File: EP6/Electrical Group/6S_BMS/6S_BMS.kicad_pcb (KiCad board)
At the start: 4 copper layers, 100 x 70 mm, 180 parts, among them IC1 DZDH0401DW-7, J1 Cell Pads, J2 24V_OUT, J3 CHARGE, J4 HVB_Front_Panel, J5 UART, J6 I2C, J7 SWD, J8 USB_C_stm32, Q1 HSBA3119, Q10 SI2301CDS-T1-GE3, Q11 SI2301CDS-T1-GE3, Q12 SI2301CDS-T1-GE3, Q13 2N7002, Q14 AO3401A, Q2 2N7002, Q3 2N7002, Q4 HSBA3119, Q5 2N7002, Q6 HSBA3119, Q7 SI2301CDS-T1-GE3, Q8 SI2301CDS-T1-GE3, Q9 SI2301CDS-T1-GE3, SW1 RESET, U1 BQ7693003, U2 TCAN1042VDRQ1, U3 STM32F103C8Tx, U4 LM66100DCK, U5 CAT24C256, U6 78L05G-AB3-R, U7 HT7533, Y1 8MHz X49SM8MSD2SC

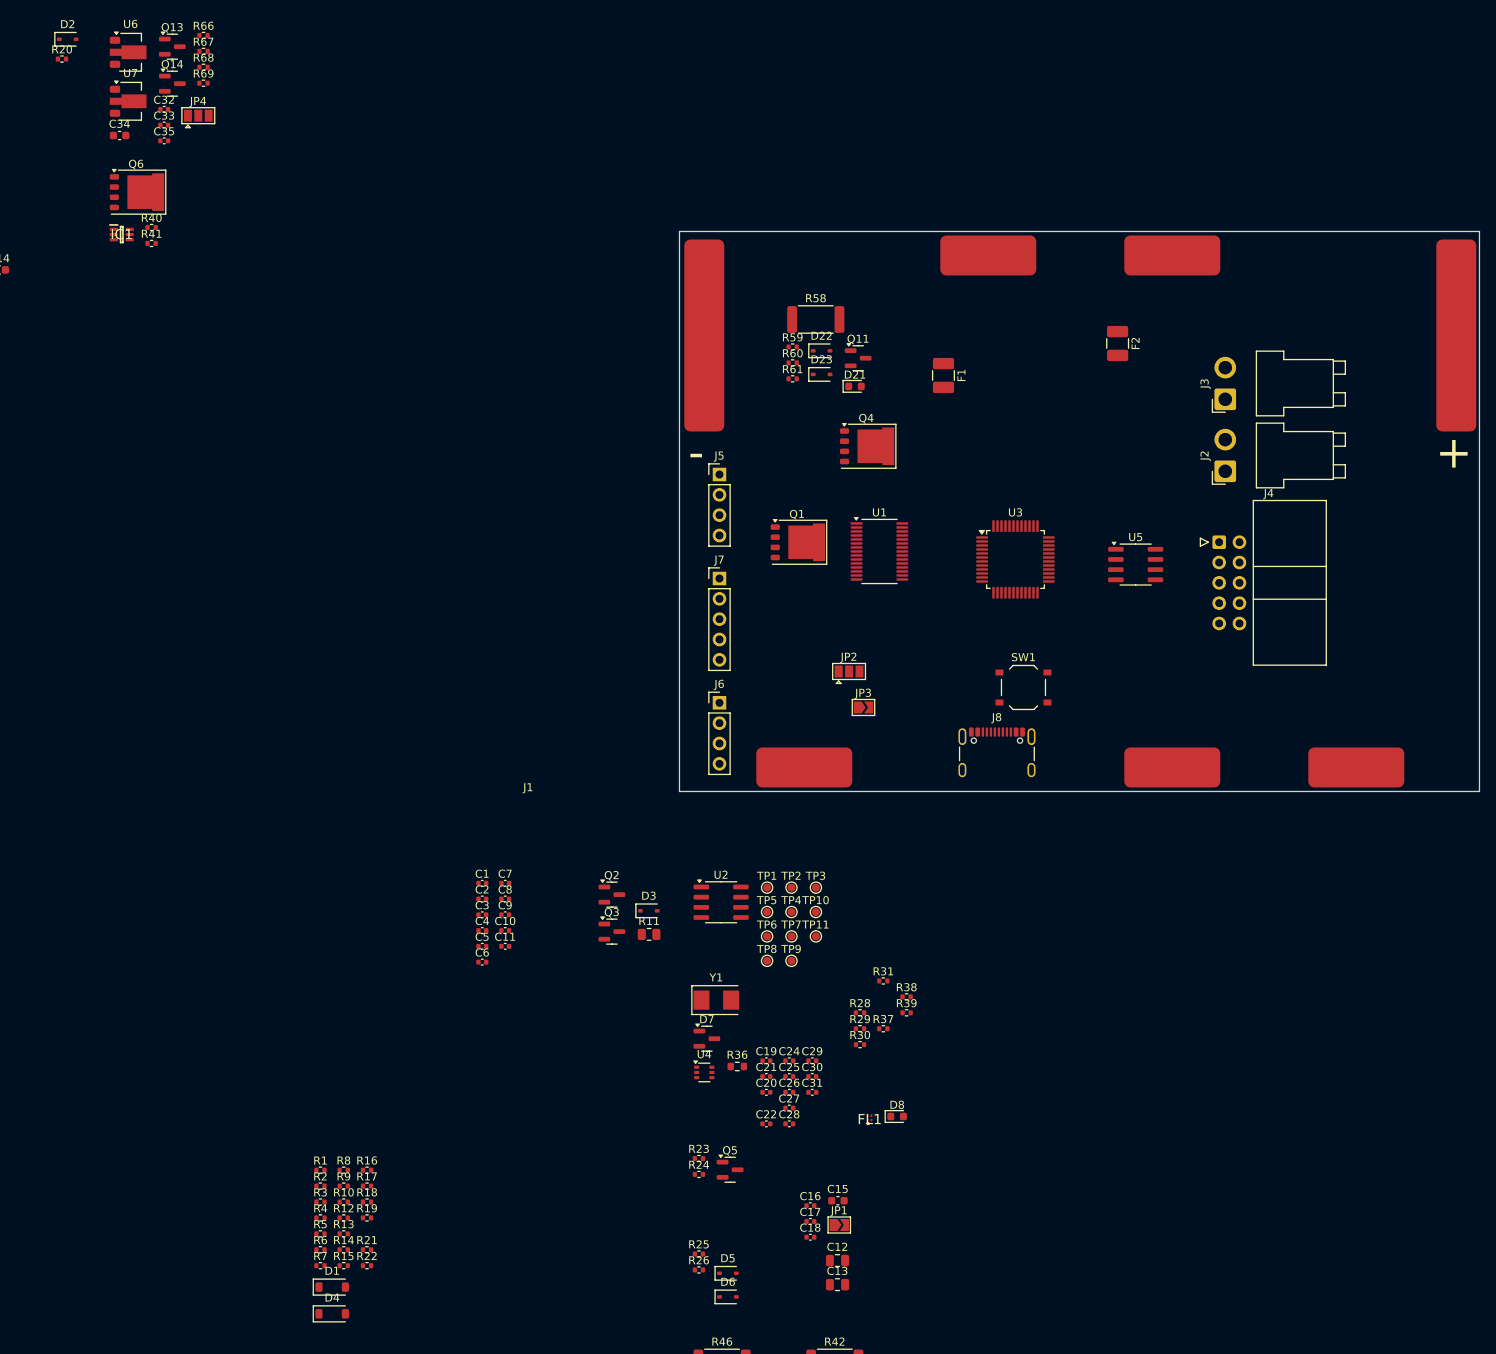
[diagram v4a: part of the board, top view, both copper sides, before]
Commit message: fix net ties and net classes
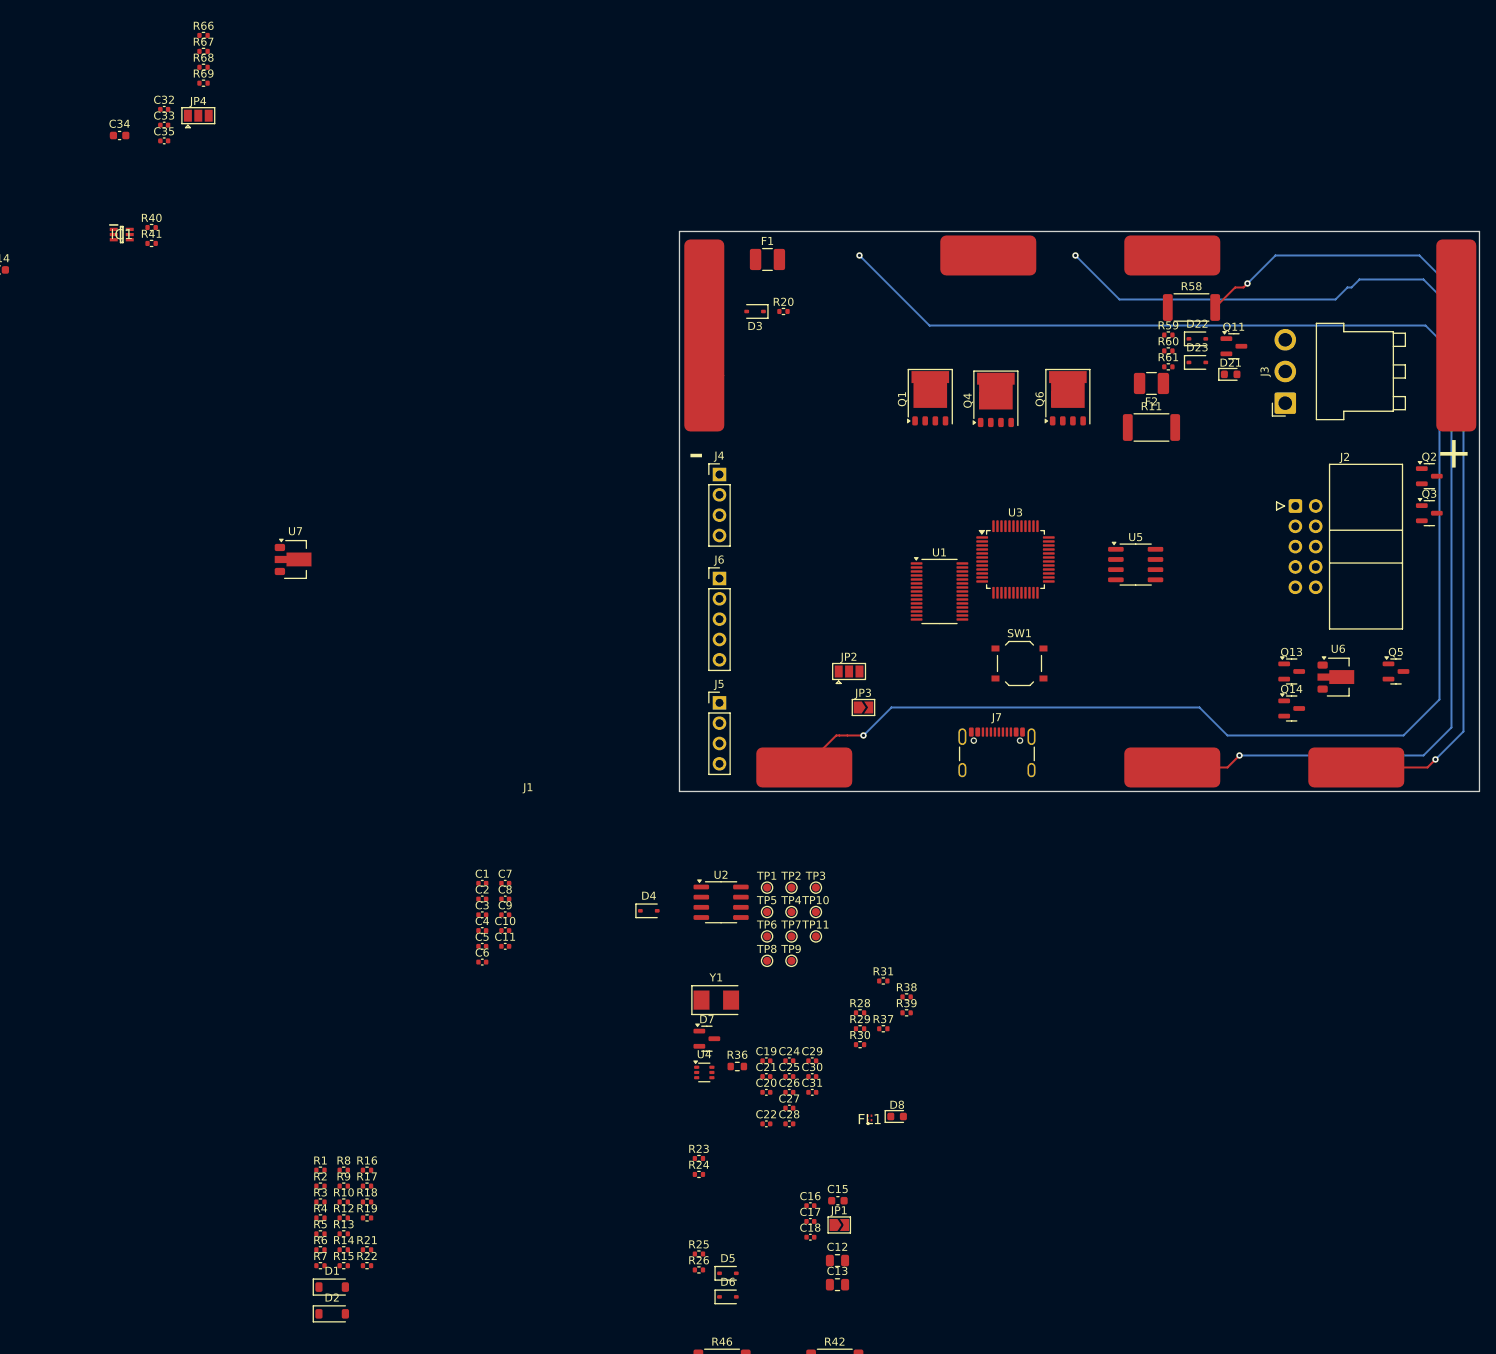
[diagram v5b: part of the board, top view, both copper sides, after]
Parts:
- removed the J4 at (167.5, 63.8)
- J2: value 24V_OUT -> Front Panel; footprint Connector_JST:JST_VH_B2PS-VH_1x02_P3.96mm_Horizontal -> Connector_IDC:IDC-Header_2x05_P2.54mm_Horizontal
- J3: value CHARGE -> Power; footprint Connector_JST:JST_VH_B2PS-VH_1x02_P3.96mm_Horizontal -> Connector_JST:JST_VH_B3PS-VH_1x03_P3.96mm_Horizontal
- R11: value 10R 1% -> 1m; footprint Resistor_SMD:R_0805_2012Metric -> Resistor_SMD:R_2512_6332Metric
- U6: value 78L05G-AB3-R -> L78L05_SOT89
- moved U6 170.0 mm to (182.3, 80.7)
- moved Q13 160.2 mm to (176.5, 80.0)
- moved Q14 160.2 mm to (176.5, 84.6)
- moved Q6 119.3 mm to (148.6, 46.0), turned to 90 degrees
- moved Q2 114.8 mm to (193.7, 55.6)
- moved Q3 114.8 mm to (193.7, 60.2)
- moved Q5 104.0 mm to (189.6, 80.0)
- moved R20 95.5 mm to (113.0, 35.0)
- moved D3 92.4 mm to (109.5, 35.0), turned to 180 degrees
- moved R11 89.2 mm to (159.0, 49.5)
- moved U7 60.9 mm to (52.0, 66.0)
- moved D22 47.0 mm to (164.7, 38.4)
- moved D23 47.0 mm to (164.7, 41.4)
- moved R59 47.0 mm to (161.1, 37.9)
- moved R60 47.0 mm to (161.1, 39.9)
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- renumbered D4 to D2, D2 to D3, D3 to D4, J5 to J4, J6 to J5, J7 to J6, J8 to J7
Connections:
- D1 pad 1: +24V -> /PACK+
- D5 pad 2: /AFE/VC5 -> /C3
- D6 pad 2: /AFE/VC10 -> /C6
- IC1 pad 4: +24V -> /PACK+
- J2 pad 1: /PACK- -> /MODE_BTN_A
- J2 pad 2: +24V -> /MODE_BTN_B
- J3 pad 2: /CHG_EXT -> /PACK+
- J5 pad 3: /MCU/I2C1_SCL -> /SCL
- J5 pad 4: /MCU/I2C1_SDA -> /SDA
- Q4 pad D: +24V -> /PACK+
- Q6 pad S: +24V -> /PACK+
- R11 pad 1: /CELLS- -> /CT0
- R9 pad 1: /CELLS- -> /CT0
- TP6 pad 1: /DISP_CS -> /MCU/SPI2_CS
- TP7 pad 1: /DISP_CLK -> /MCU/SPI2_SCK
- TP9 pad 1: /DISP_DIN -> /MCU/SPI2_MOSI
- U1 pad 16: /AFE/VC10 -> /C6
- U1 pad 22: /AFE/VC5 -> /C3
- U3 pad 25: /DISP_CS -> /MCU/SPI2_CS
- U3 pad 26: /DISP_CLK -> /MCU/SPI2_SCK
- U3 pad 28: /DISP_DIN -> /MCU/SPI2_MOSI
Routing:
- net /CT5: track 0.00 -> 207.7 mm, vias 0 -> 2
- net /CT3: track 0.00 -> 141.2 mm, vias 0 -> 2
- net /CT1: track 0.00 -> 105.3 mm, vias 0 -> 2
- net /CT6: track 0.00 -> 5.99 mm
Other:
- copper layers 4 -> 2

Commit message: switched back to xt60, changed shunt resistor
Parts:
- removed the J3 at (175.7, 46.5)
- added J2: Power Out, Connector_AMASS:AMASS_XT60PW-F_1x02_P7.20mm_Horizontal, F.Cu at (169.2, 65.0)
- added J4: Charge, Connector_AMASS:AMASS_XT60PW-M_1x02_P7.20mm_Horizontal, F.Cu at (169.2, 75.8)
- added NT1: NetTie_2, NetTie:NetTie-2_SMD_Pad0.5mm, B.Cu at (13.6, 56.9)
- C1, C10, C11, C12, C13, C14, C15, C16, C17, C18, C19, C2, C20, C21, C22, C23, C24, C25, C26, C27, C28, C29, C3, C30, C31, C32, C33, C34, C35, C4, C5, C6, C7, C8, C9, D1, D10, D11, D12, D13, D14, D15, D16, D17, D18, D19, D2, D20, D21, D22, D23, D24, D25, D26, D3, D4, D5, D6, D7, D8, D9, FL1, IC1, JP1, JP2, JP3, JP4, Q1, Q10, Q11, Q12, Q13, Q14, Q2, Q3, Q4, Q5, Q6, Q7, Q8, Q9, R1, R10, R12, R13, R14, R15, R16, R17, R18, R19, R2, R20, R21, R22, R23, R24, R25, R26, R27, R28, R29, R3, R30, R31, R32, R33, R34, R35, R36, R37, R38, R39, R4, R40, R41, R42, R43, R44, R45, R46, R47, R48, R49, R5, R50, R51, R52, R53, R54, R55, R56, R57, R58, R59, R6, R60, R61, R62, R63, R64, R65, R66, R67, R68, R69, R7, R8, R9, SW1, TP1, TP10, TP11, TP2, TP3, TP4, TP5, TP6, TP7, TP8, TP9, U1, U2, U3, U4, U5, U6, U7, Y1: moved to B.Cu
- J8: renamed from J7; moved to B.Cu
- R11: value 1m -> 10m; moved to B.Cu
- moved R27 240.1 mm to (241.1, 29.5), turned to 180 degrees
- moved R32 240.1 mm to (241.1, 31.5), turned to 180 degrees
- moved R33 240.1 mm to (241.1, 33.5), turned to 180 degrees
- moved R34 240.1 mm to (241.1, 35.5), turned to 180 degrees
- moved R35 240.1 mm to (241.1, 37.5), turned to 180 degrees
- moved C23 234.4 mm to (238.2, 36.2), turned to 180 degrees
- moved C14 212.1 mm to (227.1, 29.8), turned to 180 degrees
- moved C34 182.0 mm to (212.0, 13.0), turned to 180 degrees
- moved Q2 181.9 mm to (12.0, 61.9), turned to 180 degrees
- moved Q3 181.9 mm to (12.0, 66.5), turned to 180 degrees
- moved IC1 181.5 mm to (211.8, 25.4), turned to 180 degrees
- moved R40 174.0 mm to (208.0, 24.5), turned to 180 degrees
- moved R41 174.0 mm to (208.0, 26.5), turned to 180 degrees
- moved C32 170.9 mm to (206.5, 9.73), turned to 180 degrees
- moved C33 170.9 mm to (206.5, 11.7), turned to 180 degrees
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- renumbered J2 to J3, J4 to J5, J5 to J6, J6 to J7
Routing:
- net /CT5: track 207.7 -> 9.06 mm, vias 2 -> 1
- net /CT3: track 141.2 -> 0.00 mm, vias 2 -> 0
- net /CT1: track 105.3 -> 0.00 mm, vias 2 -> 0
- net /CT6: track 5.99 -> 0.00 mm

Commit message: Board kinda done
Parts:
- removed J5: UART, Connector_PinHeader_2.54mm:PinHeader_1x04_P2.54mm_Vertical
- removed J6: I2C, Connector_PinHeader_2.54mm:PinHeader_1x04_P2.54mm_Vertical
- removed J7: SWD, Connector_PinHeader_2.54mm:PinHeader_1x05_P2.54mm_Vertical
- removed NT1: NetTie_2, NetTie:NetTie-2_SMD_Pad0.5mm
- removed Q5: 2N7002, Package_TO_SOT_SMD:SOT-23
- removed R31: 10k, Resistor_SMD:R_0402_1005Metric
- removed TP10: UART1_TX, TestPoint:TestPoint_Pad_D1.0mm
- removed TP11: UART1_RX, TestPoint:TestPoint_Pad_D1.0mm
- added C36: 1u, Capacitor_SMD:C_0402_1005Metric, B.Cu at (129.8, 40.0)
- added C37: 1u, Capacitor_SMD:C_0402_1005Metric, B.Cu at (124.9, 38.7)
- added D27: MMSZ5246B, Diode_SMD:D_SOD-123, B.Cu at (181.8, 54.8)
- added D28: MMSZ5246B, Diode_SMD:D_SOD-123, B.Cu at (184.2, 63.5)
- added J9: STDC14, nturt_kicad_lib_EP6:box_header_14P_pitch127, F.Cu at (116.8, 28.0)
- added R70: 0R, Resistor_SMD:R_0805_2012Metric_Pad1.20x1.40mm_HandSolder, F.Cu at (107.2, 55.8)
- added R71: 100R, Resistor_SMD:R_0603_1608Metric, B.Cu at (108.2, 33.8)
- added R72: 100R, Resistor_SMD:R_0402_1005Metric, B.Cu at (156.2, 46.8)
- added TP12: REGOUT, TestPoint:TestPoint_Pad_D1.0mm, F.Cu at (140.8, 54.0)
- added U8: XC6206PxxxMR, Package_TO_SOT_SMD:SOT-23-3, B.Cu at (126.5, 40.9)
- C14, D12, D15, D18, D21, D24, D8, D9, J8, JP1, JP2, JP3, R32, R33, SW1, TP1, TP2, TP3, TP4, TP6, TP7, TP8, TP9: moved to F.Cu
- C32, C33: value 1u -> 0u1
- C34: value 10u -> 1u; footprint Capacitor_SMD:C_0603_1608Metric -> Capacitor_SMD:C_0402_1005Metric
- C35: value 10u -> 1u
- JP4: value 3V3 select -> 3V3_LDO; footprint Jumper:SolderJumper-3_P1.3mm_Open_Pad1.0x1.5mm -> Jumper:SolderJumper-2_P1.3mm_Open_TrianglePad1.0x1.5mm; moved to F.Cu
- TP5: value CAN1_S -> CAN1_STB; moved to F.Cu
- U4: value LM66100DCK -> CAT24C256; footprint Package_TO_SOT_SMD:SOT-363_SC-70-6 -> Package_SO:SOIC-8_3.9x4.9mm_P1.27mm
- U5: value CAT24C256 -> LM66100DCK; footprint Package_SO:SOIC-8_3.9x4.9mm_P1.27mm -> Package_TO_SOT_SMD:SOT-363_SC-70-6
- U6: value L78L05_SOT89 -> SN74LVC8T245; footprint Package_TO_SOT_SMD:SOT-89-3 -> Package_SO:TSSOP-24_4.4x7.8mm_P0.65mm
- U7: value HT7533 -> L78L05_SOT89
- moved Q3 174.6 mm to (186.6, 68.5)
- moved Q2 168.0 mm to (179.7, 51.3), turned to 90 degrees
- moved R27 129.3 mm to (113.8, 51.8), turned to 0 degrees
- moved C23 125.6 mm to (113.8, 53.2)
- moved R34 125.4 mm to (115.8, 37.2), turned to 0 degrees
- moved R35 125.3 mm to (115.8, 38.2), turned to 0 degrees
- moved R65 122.7 mm to (114.1, 71.8), turned to -90 degrees
- moved R33 120.6 mm to (121.5, 49.0), turned to 90 degrees
- moved R64 119.8 mm to (115.3, 72.4), turned to -90 degrees
- moved R32 119.4 mm to (123.0, 49.0), turned to 90 degrees
- moved R63 119.4 mm to (112.8, 72.4), turned to -90 degrees
- moved R53 117.7 mm to (138.7, 71.8), turned to -90 degrees
- moved D24 117.5 mm to (112.2, 75.2), turned to -90 degrees
- moved D17 117.3 mm to (148.2, 66.1), turned to 90 degrees
- moved D26 117.1 mm to (134.9, 66.1), turned to 90 degrees
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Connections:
- net /CT0 renamed CELL-
- net /CT1 renamed /Balance Node 5/cell-
- net /CT2 renamed /Balance Node 4/cell-
- net /CT4 renamed /Balance Node 2/cell-
- net /CT5 renamed /Balance Node 1/cell-
- net Net-(Q1-PadS) renamed /COMMON_S
- C32 pad 1: GND -> +3V3
- C32 pad 2: Net-(Q14-D) -> GND
- C33 pad 1: GND -> +5V
- C33 pad 2: +5V -> GND
- C34 pad 2: +5V -> Net-(Q14-D)
- C35 pad 2: +3V3LDO -> +5V
- D1 pad 2: GND -> /PACK-
- D10 pad 1: /CT6 -> /Balance Node 1/cell+
- D2 pad 2: GND -> /PACK-
- D8 pad 1: Net-(D8-K) -> GND
- D8 pad 2: /MCU/LED -> Net-(D8-A)
- F1 pad 1: /CT6 -> /CELLS+
- F1 pad 2: /CELLS+ -> /Balance Node 1/cell+
- J1 pad 7: /CT6 -> /Balance Node 1/cell+
- J2 pad 1: /PACK+ -> /PACK-
- J2 pad 2: /PACK- -> /PACK+
- J3 pad 1: /MODE_BTN_A -> /DISP_CS
- J3 pad 10: /DISP_CLK -> /MODE_BTN_A
- J3 pad 2: /MODE_BTN_B -> /DISP_CLK
- J3 pad 3: GND -> /DISP_DIN
- J3 pad 4: +5V -> /MCU_RST
- J3 pad 5: /CANH -> GND
- J3 pad 6: /MCU_RST -> /CANL
- J3 pad 7: /CANL -> /CANH
- J3 pad 8: /DISP_CS -> +5V
- J3 pad 9: /DISP_DIN -> /MODE_BTN_B
- J4 pad 1: /CHG_EXT -> /PACK-
- J4 pad 2: /PACK- -> /CHG_EXT
- JP4 pad 1: +3V3LDO -> +3V3
- JP4 pad 2: +3V3 -> +3V3LDO
- Q2 pad 2: GND -> /PACK-
- Q3 pad 2: GND -> /PACK-
- Q7 pad 2: /CT6 -> /Balance Node 1/cell+
- R1 pad 1: /CT6 -> /Balance Node 1/cell+
- R15 pad 2: GND -> /PACK-
- R16 pad 2: GND -> /PACK-
- R32 pad 2: /MCU/I2C1_SCL -> /SCL
- R33 pad 2: /MCU/I2C1_SDA -> /SDA
- R36 pad 1: Net-(D8-K) -> /MCU/LED
- R36 pad 2: GND -> Net-(D8-A)
- R37 pad 2: Net-(U4-ST) -> Net-(U5-ST)
- R40 pad 2: GND -> /PACK-
- R41 pad 2: GND -> /PACK-
- R44 pad 2: /CT6 -> /Balance Node 1/cell+
- SW1 pad 1: GND -> /MCU_RST
- SW1 pad 2: /MCU_RST -> GND
- TP1 pad 1: /MCU/I2C1_SCL -> /SCL
- TP2 pad 1: /MCU/I2C1_SDA -> /SDA
- TP5 pad 1: /MCU/CAN1_S -> /MCU/CAN1_STB
- U3 pad 12: /MCU/UART2_TX -> /MCU/USART2_TX
- U3 pad 13: /MCU/UART2_RX -> /MCU/USART2_RX
- U3 pad 14: unconnected-(U3-PA4-Pad14) -> /ALERT
- U3 pad 15: /ALERT -> unconnected-(U3-PA5-Pad15)
- U3 pad 16: /MODE_CTL -> unconnected-(U3-PA6-Pad16)
- U3 pad 21: /MCU/CAN1_S -> unconnected-(U3-PB10-Pad21)
- U3 pad 30: /MCU/UART1_TX -> unconnected-(U3-PA9-Pad30)
- U3 pad 31: /MCU/UART1_RX -> unconnected-(U3-PA10-Pad31)
- U3 pad 39: unconnected-(U3-PB3-Pad39) -> /MCU/CAN1_STB
- U3 pad 40: unconnected-(U3-PB4-Pad40) -> /MODE_CTL
- U3 pad 42: /MCU/I2C1_SCL -> /SCL
- U3 pad 43: /MCU/I2C1_SDA -> /SDA
- U4 pad 1: VBUS -> unconnected-(U4-A0-Pad1)
- U4 pad 2: GND -> unconnected-(U4-A1-Pad2)
- U4 pad 3: Net-(JP3-A) -> unconnected-(U4-A2-Pad3)
- U4 pad 4: unconnected-(U4-NC-Pad4) -> GND
- U4 pad 5: Net-(U4-ST) -> /SDA
- U4 pad 6: Net-(JP3-A) -> /SCL
- U5 pad 1: unconnected-(U5-A0-Pad1) -> VBUS
- U5 pad 2: unconnected-(U5-A1-Pad2) -> GND
- U5 pad 3: unconnected-(U5-A2-Pad3) -> Net-(JP3-A)
- U5 pad 4: GND -> unconnected-(U5-NC-Pad4)
- U5 pad 5: /MCU/I2C1_SDA -> Net-(U5-ST)
- U5 pad 6: /MCU/I2C1_SCL -> Net-(JP3-A)
- U6 pad 3: Net-(Q14-D) -> unconnected-(U6-A1-Pad3)
- U7 pad 1: GND -> +5V
- U7 pad 2: +5V -> GND
- U7 pad 3: +3V3LDO -> Net-(Q14-D)
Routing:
- net /Balance Node 4/cell-: track 0.00 -> 176.0 mm, vias 0 -> 1
- net /Balance Node 2/cell-: track 0.00 -> 132.9 mm, vias 0 -> 1
- net CELL-: track 0.00 -> 120.5 mm, vias 0 -> 9
- net +3V3: track 0.00 -> 108.4 mm, vias 0 -> 6
- net +5V: track 0.00 -> 96.2 mm, vias 0 -> 7
- net /MCU_RST: track 0.00 -> 95.0 mm, vias 0 -> 2
- net /Balance Node 1/cell+: track 0.00 -> 91.5 mm, vias 0 -> 1
- net /MODE_CTL: track 0.00 -> 73.1 mm, vias 0 -> 2
- net /CELLS+: track 0.00 -> 67.6 mm, vias 0 -> 9
- net /DSC_EN: track 0.00 -> 63.3 mm, vias 0 -> 2
- net GND: track 0.00 -> 62.9 mm, vias 0 -> 68
- net /Balance Node 1/cell-: track 9.06 -> 68.4 mm, vias 1 -> 3
- net /MCU/SPI2_CS: track 0.00 -> 57.5 mm, vias 0 -> 1
- net /MCU/SPI2_SCK: track 0.00 -> 55.4 mm, vias 0 -> 1
- net /MCU/SPI2_MOSI: track 0.00 -> 53.1 mm, vias 0 -> 1
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- added copper zone on B.Cu, net +3V3
- added copper zone on F.Cu, net /Balance Node 1/cell+
- added copper zone on B.Cu, net /CELLS+
- added copper zone on F.Cu, net /CELLS+
- added copper zone on F.Cu, net /CHG_EXT
- added copper zone on B.Cu, net /COMMON_S
- added copper zone on B.Cu, net /EXT Ideal Diode/A
- added copper zone on F.Cu, net /EXT Ideal Diode/A
- added copper zone on B.Cu, net /PACK+
- added copper zone on B.Cu, net /PACK-
- added copper zone on F.Cu, net /PACK-
- added copper zone on B.Cu, net /VC5X
- added copper zone on B.Cu, net CELL-
- added copper zone on F.Cu, net CELL-
- added copper zone on B.Cu, net GND
- added copper zone on F.Cu, net GND
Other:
- board text added: "0"
- board text added: "1"
- board text added: "2"
- board text added: "24V OUT 10A MAX"
- board text added: "3"
- board text added: "3V3"
- board text added: "4"
- board text added: "5"
- board text added: "6"
- board text added: "BOOT0"
- board text added: "CELL FUSE"
- board text added: "CHARGE/ EXTERNAL"
- board text added: "DEBUG"
- board text added: "EXT 10A FUSE"
- board text added: "FRONT PANEL"
- board text added: "I2C Pullups"
- board text added: "LDO"
- board text added: "LED"
- board text added: "REGSRC"
- board text added: "VUSB"
